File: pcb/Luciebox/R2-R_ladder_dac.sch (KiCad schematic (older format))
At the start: 25 parts, among them T2 terminal_8x1

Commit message: pcb progress dedicated R-2R ladder'
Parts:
- removed R28, R29, R30, R31, R32, R33, R34, R35, R36, R37, R38, R39, R40, R41, R42, R43: R_Small, Luciebox:1206, symbol Device:R_Small
- added R28: DAC_R-2R, Luciebox:SIP-10, symbol Luciebox_components:DAC_R-2R
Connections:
- net DAC_analog: now also R28.1
- net GND: now also R28.10 (RT)
- net at R20.1, T2.8: now also R28.2 (MSB)
- net at R27.1, T2.1: now also R28.9 (LSB)
- net at R26.1, T2.2: now also R28.8
- net at R25.1, T2.3: now also R28.7
- net at R24.1, T2.4: now also R28.6
- net at R23.1, T2.5: now also R28.5
- net at R22.1, T2.6: now also R28.4
- net at R21.1, T2.7: now also R28.3

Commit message: working on pcb of luciebox
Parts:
- added T? (x2): terminal_8x1, Luciebox:Terminal_8x1_100mil, symbol Luciebox_components:terminal_8x1
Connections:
- net GND: now also T?.1, T?.2, T?.3, T?.4, T?.5, T?.6, T?.7, T?.8
- new net VCC: T?.1, T?.2, T?.3, T?.4, T?.5, T?.6, T?.7, T?.8
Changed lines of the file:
@@
 $EndComp
-Wire Wire Line
-	3850 1900 3500 1900
-Wire Wire Line
-	3500 1900 3500 2100
 Wire Wire Line
 	2750 2300 2750 2350
@@
 Connection ~ 2850 3100
 Connection ~ 2750 3100
+$Comp
+L Luciebox_components:terminal_8x1 T?
+U 1 1 5DAEA72B
+P 3300 1700
+AR Path="/5D74964C/5DAEA72B" Ref="T?"  Part="1"
+AR Path="/5D761BCA/5DAEA72B" Ref="T?"  Part="1"
+AR Path="/5D9307E8/5DAEA72B" Ref="T?"  Part="1"
+F 0 "T?" V 3815 2300 50  0000 C CNN
+F 1 "terminal_8x1" V 3724 2300 50  0000 C CNN
+F 2 "Luciebox:Terminal_8x1_100mil" H 3300 1700 50  0001 C CNN
+F 3 "" H 3300 1700 50  0001 C CNN
+	1    3300 1700
+	0    -1   -1   0
+$EndComp
+Connection ~ 2600 2100
+Wire Wire Line
+	2700 1900 2750 1900
+Wire Wire Line
+	2750 1900 2750 2100
+Wire Wire Line
+	2800 2050 2900 2050
+Wire Wire Line
+	2900 2050 2900 2100
+Wire Wire Line
+	2900 2000 3050 2000
+Wire Wire Line
+	3050 2000 3050 2100
+Wire Wire Line
+	3000 1950 3200 1950
+Wire Wire Line
+	3200 1950 3200 2100
+Wire Wire Line
+	2600 1750 2600 2100
+Wire Wire Line
+	2700 1900 2700 1750
+Wire Wire Line
+	2800 1750 2800 2050
+Wire Wire Line
+	2900 1750 2900 2000
+Wire Wire Line
+	3000 1750 3000 1950
+Wire Wire Line
+	3100 1750 3100 1900
+Wire Wire Line
+	3100 1900 3350 1900
+Wire Wire Line
+	3350 1900 3350 2100
+Wire Wire Line
+	3200 1750 3200 1850
+Wire Wire Line
+	3200 1850 3500 1850
+Wire Wire Line
+	3500 1850 3500 2100
+Wire Wire Line
+	3300 1750 3300 1800
+Wire Wire Line
+	3300 1800 3650 1800
+Wire Wire Line
+	3650 1800 3650 2100
+Connection ~ 3650 2100
+Wire Wire Line
+	3850 1900 3750 1900
+Wire Wire Line
+	3750 1900 3750 2100
+Wire Wire Line
+	3750 2100 3650 2100
+$Comp
+L Luciebox_components:terminal_8x1 T?
+U 1 1 5DB0039D
+P 3300 950
+AR Path="/5D74964C/5DB0039D" Ref="T?"  Part="1"
+AR Path="/5D761BCA/5DB0039D" Ref="T?"  Part="1"
+AR Path="/5D9307E8/5DB0039D" Ref="T?"  Part="1"
+F 0 "T?" V 3815 1550 50  0000 C CNN
+F 1 "terminal_8x1" V 3724 1550 50  0000 C CNN
+F 2 "Luciebox:Terminal_8x1_100mil" H 3300 950 50  0001 C CNN
+F 3 "" H 3300 950 50  0001 C CNN
+	1    3300 950
+	0    -1   -1   0
+$EndComp
+Wire Wire Line
+	3300 1000 3200 1000
+Connection ~ 2700 1000
+Wire Wire Line
+	2700 1000 2600 1000
+Connection ~ 2800 1000
+Wire Wire Line
+	2800 1000 2700 1000
+Connection ~ 2900 1000
+Wire Wire Line
+	2900 1000 2800 1000
+Connection ~ 3000 1000
+Wire Wire Line
+	3000 1000 2900 1000
+Connection ~ 3100 1000
+Wire Wire Line
+	3100 1000 3000 1000
+Connection ~ 3200 1000
+Wire Wire Line
+	3200 1000 3100 1000
+Wire Wire Line
+	3300 1000 3400 1000
+Connection ~ 3300 1000
+$Comp
+L power:VCC #PWR?
+U 1 1 5DB05874
+P 3400 1000
+F 0 "#PWR?" H 3400 850 50  0001 C CNN
+F 1 "VCC" H 3417 1173 50  0000 C CNN
+F 2 "" H 3400 1000 50  0001 C CNN
+F 3 "" H 3400 1000 50  0001 C CNN
+	1    3400 1000
+	1    0    0    -1
+$EndComp
 $EndSCHEMATC

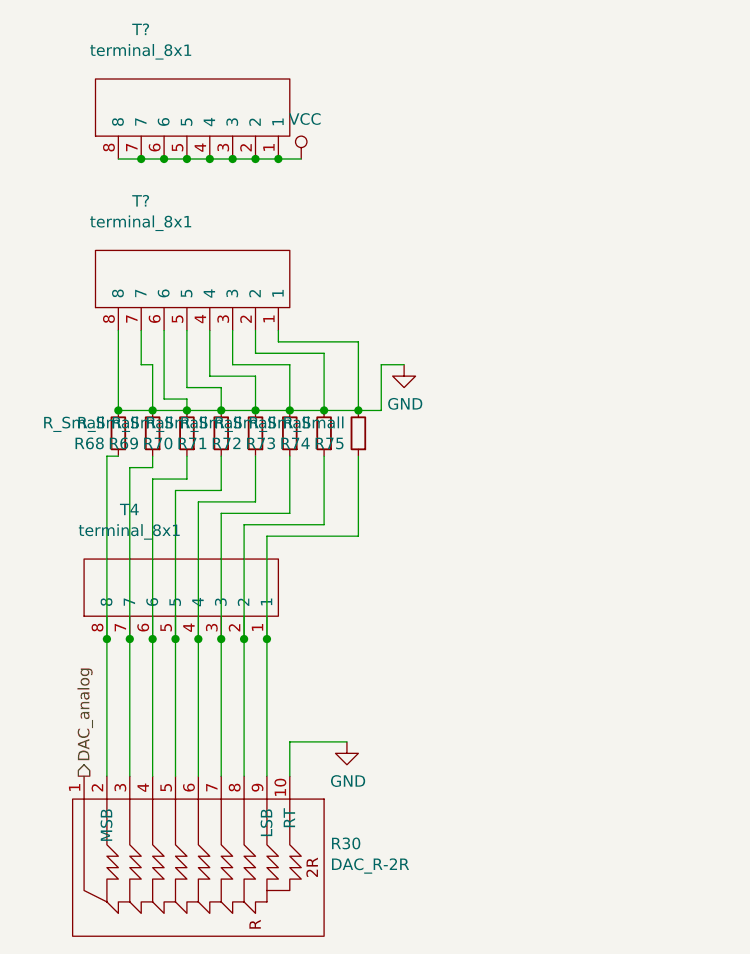
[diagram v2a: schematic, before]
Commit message: pcb add auto power OFF hardware
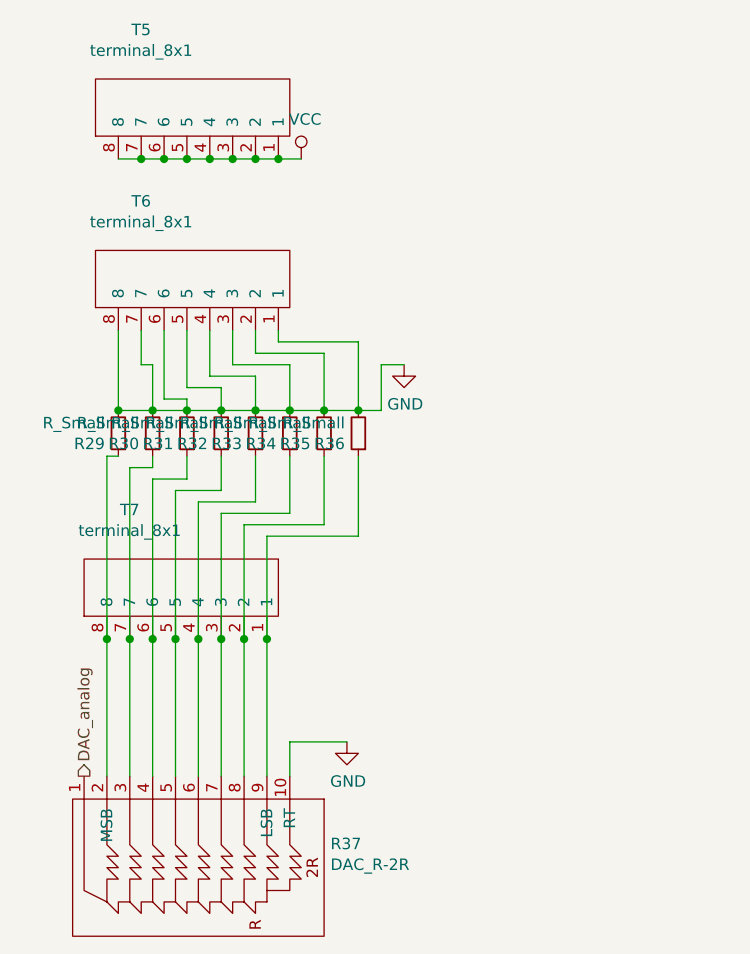
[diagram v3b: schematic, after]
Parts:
- gave numbers to parts that had none: 2
- renumbered T2 to T4
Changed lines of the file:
@@
 EESchema Schematic File Version 4
 LIBS:Luciebox-cache
-LIBS:R-2R_DAC-cache
 EELAYER 29 0
 EELAYER END
 $Descr A4 11693 8268
 encoding utf-8
-Sheet 4 4
+Sheet 3 4
 Title ""
 Date ""
@@
 P 3650 2200
 AR Path="/5D74964C/5D7526CF" Ref="R27"  Part="1"
-AR Path="/5D761BCA/5D7526CF" Ref="R51"  Part="1"
-AR Path="/5D9307E8/5D7526CF" Ref="R75"  Part="1"
-F 0 "R75" H 3709 2246 50  0000 L CNN
+AR Path="/5D761BCA/5D7526CF" Ref="R36"  Part="1"
+AR Path="/5D9307E8/5D7526CF" Ref="R45"  Part="1"
+F 0 "R36" H 3709 2246 50  0000 L CNN
 F 1 "R_Small" H 3709 2155 50  0000 L CNN
 F 2 "Luciebox:1206" H 3650 2200 50  0001 C CNN
@@
 P 3500 2200
 AR Path="/5D74964C/5D7526DB" Ref="R26"  Part="1"
-AR Path="/5D761BCA/5D7526DB" Ref="R50"  Part="1"
-AR Path="/5D9307E8/5D7526DB" Ref="R74"  Part="1"
-F 0 "R74" H 3559 2246 50  0000 L CNN
+AR Path="/5D761BCA/5D7526DB" Ref="R35"  Part="1"
+AR Path="/5D9307E8/5D7526DB" Ref="R44"  Part="1"
+F 0 "R35" H 3559 2246 50  0000 L CNN
 F 1 "R_Small" H 3559 2155 50  0000 L CNN
 F 2 "Luciebox:1206" H 3500 2200 50  0001 C CNN
@@
 P 3350 2200
 AR Path="/5D74964C/5D7526E1" Ref="R25"  Part="1"
-AR Path="/5D761BCA/5D7526E1" Ref="R49"  Part="1"
-AR Path="/5D9307E8/5D7526E1" Ref="R73"  Part="1"
-F 0 "R73" H 3409 2246 50  0000 L CNN
+AR Path="/5D761BCA/5D7526E1" Ref="R34"  Part="1"
+AR Path="/5D9307E8/5D7526E1" Ref="R43"  Part="1"
+F 0 "R34" H 3409 2246 50  0000 L CNN
 F 1 "R_Small" H 3409 2155 50  0000 L CNN
 F 2 "Luciebox:1206" H 3350 2200 50  0001 C CNN
@@
 P 3200 2200
 AR Path="/5D74964C/5D7526E7" Ref="R24"  Part="1"
-AR Path="/5D761BCA/5D7526E7" Ref="R48"  Part="1"
-AR Path="/5D9307E8/5D7526E7" Ref="R72"  Part="1"
-F 0 "R72" H 3259 2246 50  0000 L CNN
+AR Path="/5D761BCA/5D7526E7" Ref="R33"  Part="1"
+AR Path="/5D9307E8/5D7526E7" Ref="R42"  Part="1"
+F 0 "R33" H 3259 2246 50  0000 L CNN
 F 1 "R_Small" H 3259 2155 50  0000 L CNN
 F 2 "Luciebox:1206" H 3200 2200 50  0001 C CNN
@@
 P 3050 2200
 AR Path="/5D74964C/5D7526ED" Ref="R23"  Part="1"
-AR Path="/5D761BCA/5D7526ED" Ref="R47"  Part="1"
-AR Path="/5D9307E8/5D7526ED" Ref="R71"  Part="1"
-F 0 "R71" H 3109 2246 50  0000 L CNN
+AR Path="/5D761BCA/5D7526ED" Ref="R32"  Part="1"
+AR Path="/5D9307E8/5D7526ED" Ref="R41"  Part="1"
+F 0 "R32" H 3109 2246 50  0000 L CNN
 F 1 "R_Small" H 3109 2155 50  0000 L CNN
 F 2 "Luciebox:1206" H 3050 2200 50  0001 C CNN
@@
 P 2900 2200
 AR Path="/5D74964C/5D7526F3" Ref="R22"  Part="1"
-AR Path="/5D761BCA/5D7526F3" Ref="R46"  Part="1"
-AR Path="/5D9307E8/5D7526F3" Ref="R70"  Part="1"
-F 0 "R70" H 2959 2246 50  0000 L CNN
+AR Path="/5D761BCA/5D7526F3" Ref="R31"  Part="1"
+AR Path="/5D9307E8/5D7526F3" Ref="R40"  Part="1"
+F 0 "R31" H 2959 2246 50  0000 L CNN
 F 1 "R_Small" H 2959 2155 50  0000 L CNN
 F 2 "Luciebox:1206" H 2900 2200 50  0001 C CNN
@@
 P 2750 2200
 AR Path="/5D74964C/5D7526F9" Ref="R21"  Part="1"
-AR Path="/5D761BCA/5D7526F9" Ref="R45"  Part="1"
-AR Path="/5D9307E8/5D7526F9" Ref="R69"  Part="1"
-F 0 "R69" H 2809 2246 50  0000 L CNN
+AR Path="/5D761BCA/5D7526F9" Ref="R30"  Part="1"
+AR Path="/5D9307E8/5D7526F9" Ref="R39"  Part="1"
+F 0 "R30" H 2809 2246 50  0000 L CNN
 F 1 "R_Small" H 2809 2155 50  0000 L CNN
 F 2 "Luciebox:1206" H 2750 2200 50  0001 C CNN
@@
 Connection ~ 2750 2100
 $Comp
-L power:GND #PWR019
+L power:GND #PWR020
 U 1 1 5D75277B
 P 3850 1900
-AR Path="/5D74964C/5D75277B" Ref="#PWR019"  Part="1"
-AR Path="/5D761BCA/5D75277B" Ref="#PWR021"  Part="1"
-AR Path="/5D9307E8/5D75277B" Ref="#PWR023"  Part="1"
+AR Path="/5D74964C/5D75277B" Ref="#PWR020"  Part="1"
+AR Path="/5D761BCA/5D75277B" Ref="#PWR023"  Part="1"
+AR Path="/5D9307E8/5D75277B" Ref="#PWR026"  Part="1"
 F 0 "#PWR023" H 3850 1650 50  0001 C CNN
 F 1 "GND" H 3855 1727 50  0000 C CNN
@@
 P 2600 2200
 AR Path="/5D74964C/5D7527B8" Ref="R20"  Part="1"
-AR Path="/5D761BCA/5D7527B8" Ref="R44"  Part="1"
-AR Path="/5D9307E8/5D7527B8" Ref="R68"  Part="1"
-F 0 "R68" H 2659 2246 50  0000 L CNN
+AR Path="/5D761BCA/5D7527B8" Ref="R29"  Part="1"
+AR Path="/5D9307E8/5D7527B8" Ref="R38"  Part="1"
+F 0 "R29" H 2659 2246 50  0000 L CNN
 F 1 "R_Small" H 2659 2155 50  0000 L CNN
 F 2 "Luciebox:1206" H 2600 2200 50  0001 C CNN
@@
 P 2450 3700
 AR Path="/5D74964C/5DABC300" Ref="R28"  Part="1"
-AR Path="/5D761BCA/5DABC300" Ref="R29"  Part="1"
-AR Path="/5D9307E8/5DABC300" Ref="R30"  Part="1"
-F 0 "R30" V 2746 4778 50  0000 L CNN
+AR Path="/5D761BCA/5DABC300" Ref="R37"  Part="1"
+AR Path="/5D9307E8/5DABC300" Ref="R46"  Part="1"
+F 0 "R37" V 2746 4778 50  0000 L CNN
 F 1 "DAC_R-2R" V 2837 4778 50  0000 L CNN
 F 2 "Luciebox:SIP-10" H 2450 3700 50  0001 C CNN
@@
 	2550 2300 2550 3100
 $Comp
-L Luciebox_components:terminal_8x1 T2
+L Luciebox_components:terminal_8x1 T4
 U 1 1 5D7526D5
 P 3250 3050
-AR Path="/5D74964C/5D7526D5" Ref="T2"  Part="1"
-AR Path="/5D761BCA/5D7526D5" Ref="T3"  Part="1"
-AR Path="/5D9307E8/5D7526D5" Ref="T4"  Part="1"
-F 0 "T4" V 3765 3650 50  0000 C CNN
+AR Path="/5D74964C/5D7526D5" Ref="T4"  Part="1"
+AR Path="/5D761BCA/5D7526D5" Ref="T7"  Part="1"
+AR Path="/5D9307E8/5D7526D5" Ref="T10"  Part="1"
+F 0 "T7" V 3765 3650 50  0000 C CNN
 F 1 "terminal_8x1" V 3674 3650 50  0000 C CNN
 F 2 "Luciebox:Terminal_8x1_100mil" H 3250 3050 50  0001 C CNN
@@
 	3250 3100 3250 3700
 $Comp
-L power:GND #PWR0101
+L power:GND #PWR021
 U 1 1 5DACA23D
 P 3600 3550
-AR Path="/5D74964C/5DACA23D" Ref="#PWR0101"  Part="1"
-AR Path="/5D761BCA/5DACA23D" Ref="#PWR0102"  Part="1"
-AR Path="/5D9307E8/5DACA23D" Ref="#PWR0103"  Part="1"
-F 0 "#PWR0103" H 3600 3300 50  0001 C CNN
+AR Path="/5D74964C/5DACA23D" Ref="#PWR021"  Part="1"
+AR Path="/5D761BCA/5DACA23D" Ref="#PWR024"  Part="1"
+AR Path="/5D9307E8/5DACA23D" Ref="#PWR027"  Part="1"
+F 0 "#PWR024" H 3600 3300 50  0001 C CNN
 F 1 "GND" H 3605 3377 50  0000 C CNN
 F 2 "" H 3600 3550 50  0001 C CNN
@@
 Connection ~ 2750 3100
 $Comp
-L Luciebox_components:terminal_8x1 T?
+L Luciebox_components:terminal_8x1 T3
 U 1 1 5DAEA72B
 P 3300 1700
-AR Path="/5D74964C/5DAEA72B" Ref="T?"  Part="1"
-AR Path="/5D761BCA/5DAEA72B" Ref="T?"  Part="1"
-AR Path="/5D9307E8/5DAEA72B" Ref="T?"  Part="1"
-F 0 "T?" V 3815 2300 50  0000 C CNN
+AR Path="/5D74964C/5DAEA72B" Ref="T3"  Part="1"
+AR Path="/5D761BCA/5DAEA72B" Ref="T6"  Part="1"
+AR Path="/5D9307E8/5DAEA72B" Ref="T9"  Part="1"
+F 0 "T6" V 3815 2300 50  0000 C CNN
 F 1 "terminal_8x1" V 3724 2300 50  0000 C CNN
 F 2 "Luciebox:Terminal_8x1_100mil" H 3300 1700 50  0001 C CNN
@@
 	3750 2100 3650 2100
 $Comp
-L Luciebox_components:terminal_8x1 T?
+L Luciebox_components:terminal_8x1 T2
 U 1 1 5DB0039D
 P 3300 950
-AR Path="/5D74964C/5DB0039D" Ref="T?"  Part="1"
-AR Path="/5D761BCA/5DB0039D" Ref="T?"  Part="1"
-AR Path="/5D9307E8/5DB0039D" Ref="T?"  Part="1"
-F 0 "T?" V 3815 1550 50  0000 C CNN
+AR Path="/5D74964C/5DB0039D" Ref="T2"  Part="1"
+AR Path="/5D761BCA/5DB0039D" Ref="T5"  Part="1"
+AR Path="/5D9307E8/5DB0039D" Ref="T8"  Part="1"
+F 0 "T5" V 3815 1550 50  0000 C CNN
 F 1 "terminal_8x1" V 3724 1550 50  0000 C CNN
 F 2 "Luciebox:Terminal_8x1_100mil" H 3300 950 50  0001 C CNN
@@
 Connection ~ 3300 1000
 $Comp
-L power:VCC #PWR?
+L power:VCC #PWR025
 U 1 1 5DB05874
 P 3400 1000
-F 0 "#PWR?" H 3400 850 50  0001 C CNN
+AR Path="/5D9307E8/5DB05874" Ref="#PWR025"  Part="1"
+AR Path="/5D74964C/5DB05874" Ref="#PWR019"  Part="1"
+AR Path="/5D761BCA/5DB05874" Ref="#PWR022"  Part="1"
+F 0 "#PWR022" H 3400 850 50  0001 C CNN
 F 1 "VCC" H 3417 1173 50  0000 C CNN
 F 2 "" H 3400 1000 50  0001 C CNN

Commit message: all components have footprint. All fitting on board.
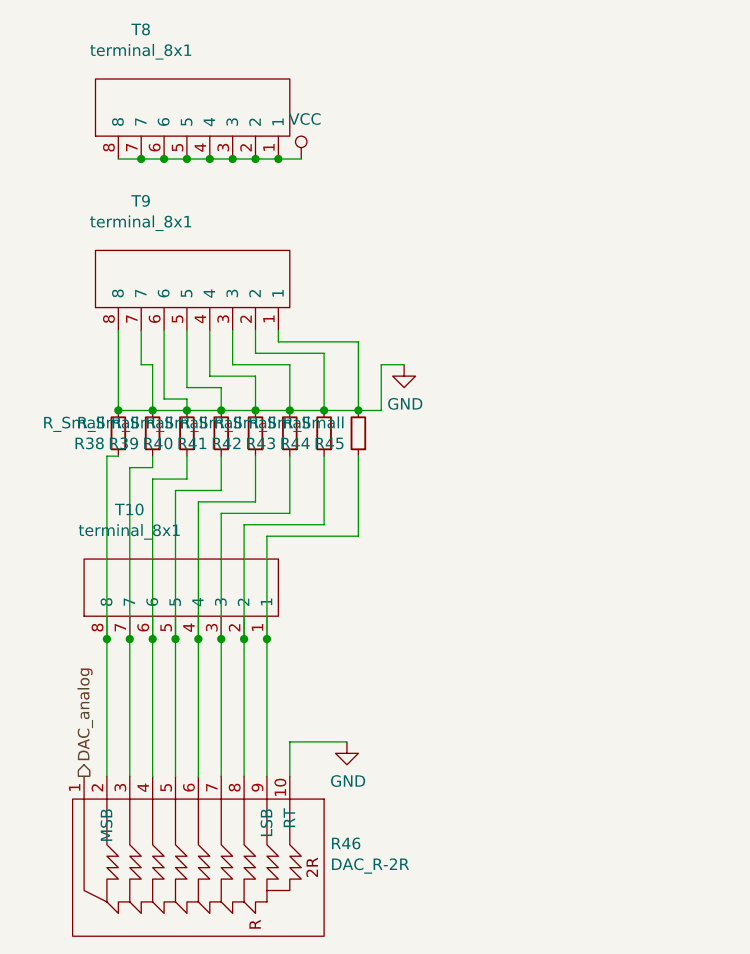
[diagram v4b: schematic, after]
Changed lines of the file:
@@
 AR Path="/5D761BCA/5D7526CF" Ref="R36"  Part="1"
 AR Path="/5D9307E8/5D7526CF" Ref="R45"  Part="1"
-F 0 "R36" H 3709 2246 50  0000 L CNN
+F 0 "R45" H 3709 2246 50  0000 L CNN
 F 1 "R_Small" H 3709 2155 50  0000 L CNN
 F 2 "Luciebox:1206" H 3650 2200 50  0001 C CNN
@@
 AR Path="/5D761BCA/5D7526DB" Ref="R35"  Part="1"
 AR Path="/5D9307E8/5D7526DB" Ref="R44"  Part="1"
-F 0 "R35" H 3559 2246 50  0000 L CNN
+F 0 "R44" H 3559 2246 50  0000 L CNN
 F 1 "R_Small" H 3559 2155 50  0000 L CNN
 F 2 "Luciebox:1206" H 3500 2200 50  0001 C CNN
@@
 AR Path="/5D761BCA/5D7526E1" Ref="R34"  Part="1"
 AR Path="/5D9307E8/5D7526E1" Ref="R43"  Part="1"
-F 0 "R34" H 3409 2246 50  0000 L CNN
+F 0 "R43" H 3409 2246 50  0000 L CNN
 F 1 "R_Small" H 3409 2155 50  0000 L CNN
 F 2 "Luciebox:1206" H 3350 2200 50  0001 C CNN
@@
 AR Path="/5D761BCA/5D7526E7" Ref="R33"  Part="1"
 AR Path="/5D9307E8/5D7526E7" Ref="R42"  Part="1"
-F 0 "R33" H 3259 2246 50  0000 L CNN
+F 0 "R42" H 3259 2246 50  0000 L CNN
 F 1 "R_Small" H 3259 2155 50  0000 L CNN
 F 2 "Luciebox:1206" H 3200 2200 50  0001 C CNN
@@
 AR Path="/5D761BCA/5D7526ED" Ref="R32"  Part="1"
 AR Path="/5D9307E8/5D7526ED" Ref="R41"  Part="1"
-F 0 "R32" H 3109 2246 50  0000 L CNN
+F 0 "R41" H 3109 2246 50  0000 L CNN
 F 1 "R_Small" H 3109 2155 50  0000 L CNN
 F 2 "Luciebox:1206" H 3050 2200 50  0001 C CNN
@@
 AR Path="/5D761BCA/5D7526F3" Ref="R31"  Part="1"
 AR Path="/5D9307E8/5D7526F3" Ref="R40"  Part="1"
-F 0 "R31" H 2959 2246 50  0000 L CNN
+F 0 "R40" H 2959 2246 50  0000 L CNN
 F 1 "R_Small" H 2959 2155 50  0000 L CNN
 F 2 "Luciebox:1206" H 2900 2200 50  0001 C CNN
@@
 AR Path="/5D761BCA/5D7526F9" Ref="R30"  Part="1"
 AR Path="/5D9307E8/5D7526F9" Ref="R39"  Part="1"
-F 0 "R30" H 2809 2246 50  0000 L CNN
+F 0 "R39" H 2809 2246 50  0000 L CNN
 F 1 "R_Small" H 2809 2155 50  0000 L CNN
 F 2 "Luciebox:1206" H 2750 2200 50  0001 C CNN
@@
 AR Path="/5D761BCA/5D75277B" Ref="#PWR023"  Part="1"
 AR Path="/5D9307E8/5D75277B" Ref="#PWR026"  Part="1"
-F 0 "#PWR023" H 3850 1650 50  0001 C CNN
+F 0 "#PWR026" H 3850 1650 50  0001 C CNN
 F 1 "GND" H 3855 1727 50  0000 C CNN
 F 2 "" H 3850 1900 50  0001 C CNN
@@
 AR Path="/5D761BCA/5D7527B8" Ref="R29"  Part="1"
 AR Path="/5D9307E8/5D7527B8" Ref="R38"  Part="1"
-F 0 "R29" H 2659 2246 50  0000 L CNN
+F 0 "R38" H 2659 2246 50  0000 L CNN
 F 1 "R_Small" H 2659 2155 50  0000 L CNN
 F 2 "Luciebox:1206" H 2600 2200 50  0001 C CNN
@@
 AR Path="/5D761BCA/5DABC300" Ref="R37"  Part="1"
 AR Path="/5D9307E8/5DABC300" Ref="R46"  Part="1"
-F 0 "R37" V 2746 4778 50  0000 L CNN
+F 0 "R46" V 2746 4778 50  0000 L CNN
 F 1 "DAC_R-2R" V 2837 4778 50  0000 L CNN
 F 2 "Luciebox:SIP-10" H 2450 3700 50  0001 C CNN
@@
 AR Path="/5D761BCA/5D7526D5" Ref="T7"  Part="1"
 AR Path="/5D9307E8/5D7526D5" Ref="T10"  Part="1"
-F 0 "T7" V 3765 3650 50  0000 C CNN
+F 0 "T10" V 3765 3650 50  0000 C CNN
 F 1 "terminal_8x1" V 3674 3650 50  0000 C CNN
 F 2 "Luciebox:Terminal_8x1_100mil" H 3250 3050 50  0001 C CNN
@@
 AR Path="/5D761BCA/5DACA23D" Ref="#PWR024"  Part="1"
 AR Path="/5D9307E8/5DACA23D" Ref="#PWR027"  Part="1"
-F 0 "#PWR024" H 3600 3300 50  0001 C CNN
+F 0 "#PWR027" H 3600 3300 50  0001 C CNN
 F 1 "GND" H 3605 3377 50  0000 C CNN
 F 2 "" H 3600 3550 50  0001 C CNN
@@
 AR Path="/5D761BCA/5DAEA72B" Ref="T6"  Part="1"
 AR Path="/5D9307E8/5DAEA72B" Ref="T9"  Part="1"
-F 0 "T6" V 3815 2300 50  0000 C CNN
+F 0 "T9" V 3815 2300 50  0000 C CNN
 F 1 "terminal_8x1" V 3724 2300 50  0000 C CNN
 F 2 "Luciebox:Terminal_8x1_100mil" H 3300 1700 50  0001 C CNN
@@
 AR Path="/5D761BCA/5DB0039D" Ref="T5"  Part="1"
 AR Path="/5D9307E8/5DB0039D" Ref="T8"  Part="1"
-F 0 "T5" V 3815 1550 50  0000 C CNN
+F 0 "T8" V 3815 1550 50  0000 C CNN
 F 1 "terminal_8x1" V 3724 1550 50  0000 C CNN
 F 2 "Luciebox:Terminal_8x1_100mil" H 3300 950 50  0001 C CNN
@@
 AR Path="/5D74964C/5DB05874" Ref="#PWR019"  Part="1"
 AR Path="/5D761BCA/5DB05874" Ref="#PWR022"  Part="1"
-F 0 "#PWR022" H 3400 850 50  0001 C CNN
+F 0 "#PWR025" H 3400 850 50  0001 C CNN
 F 1 "VCC" H 3417 1173 50  0000 C CNN
 F 2 "" H 3400 1000 50  0001 C CNN
